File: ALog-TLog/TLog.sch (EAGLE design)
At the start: 107 parts, among them IC1 ATMEGA644M, J6 5.5x2.1mm Barrel, Q11 MOSFET-NCH-BSS138, Q12 MOSFET_PCH-IRLML2244, Q5 MOSFET_PCH-IRLML2244, Q6 MOSFET_PCH-IRLML2244, Q7 MOSFET_PCH-IRLML2244, Q8 MOSFET-NCH-BSS138, Q9 MOSFET-NCH-BSS138, U2 FT231X-Q, U3 915MHz, U4 SX1509, X2 87832-14

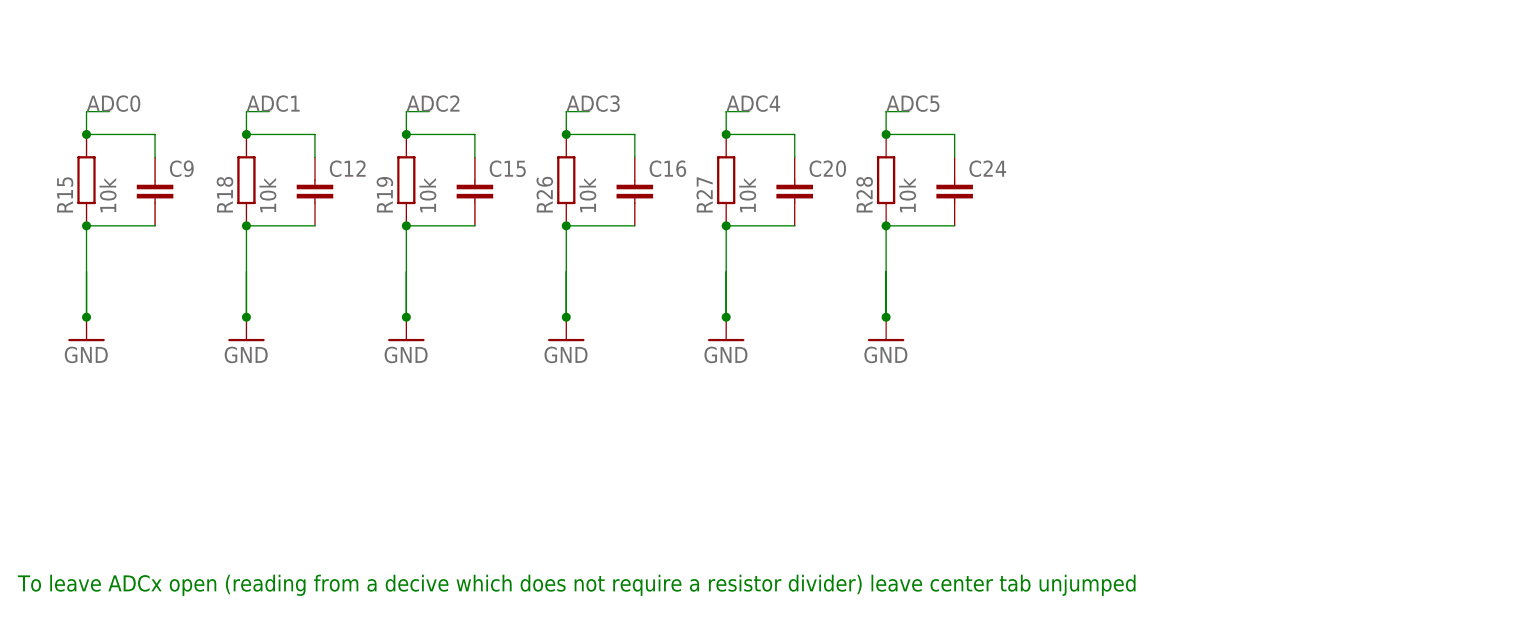
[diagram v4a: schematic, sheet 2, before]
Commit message: Issue Fix Complete
Fixed issues: #9, #12, #8

Ready for review
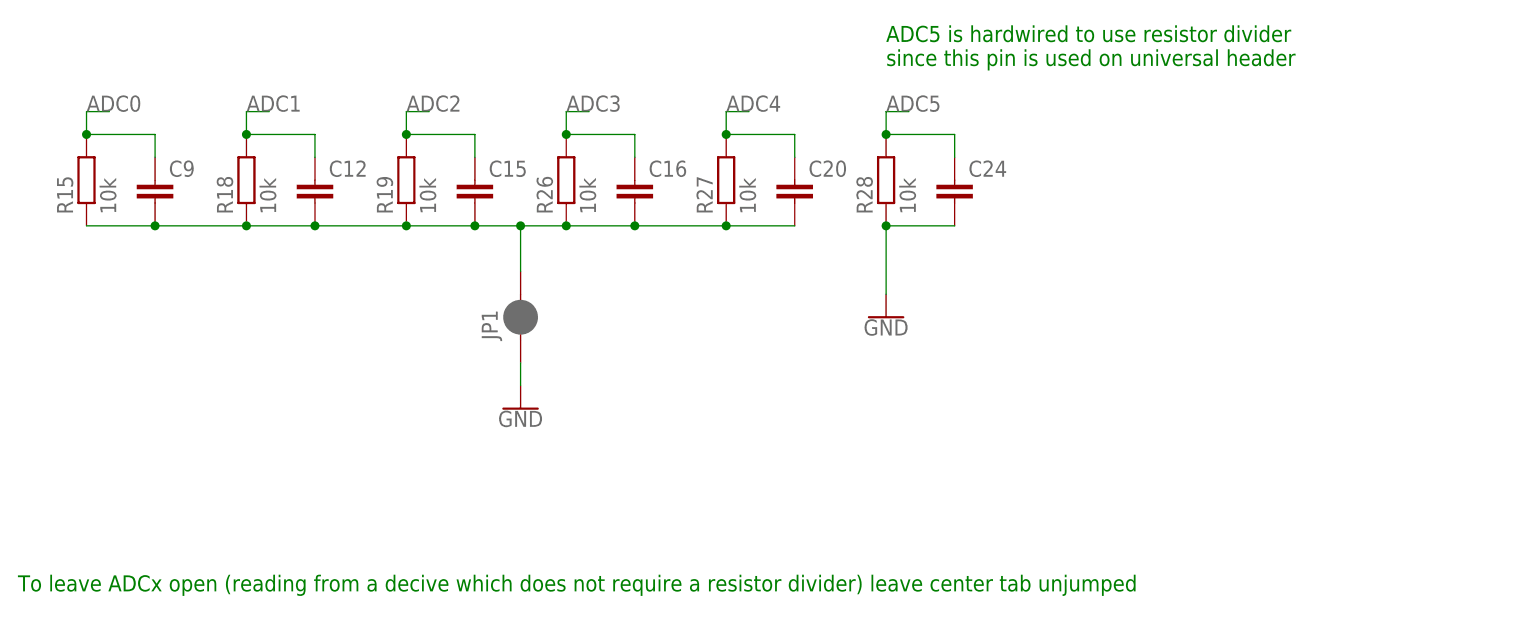
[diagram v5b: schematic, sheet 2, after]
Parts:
- added JP1: JUMPER-SMT_2_NC_PASTE_SILK, SparkFun-Jumpers:JUMPER-SMT_2_NC_PASTE_SILK
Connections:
- removed net 5V_EXT: R25.2
- new net THERM_GND: C12.2, C15.2, C16.2, C20.2, C9.2, JP1.2, R15.1, R18.1, R19.1, R26.1, R27.1
- net 5V: no longer U2.VCC
- net EXT_5V: now also R25.2
- net GND: now also JP1.1; no longer C12.2, C15.2, C16.2, C20.2, C9.2, R15.1, R18.1, R19.1, R26.1, R27.1
- net VUSB: now also U2.VCC
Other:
- note added: "ADC5 is hardwired to use resistor divider since this pin is used on universal header"
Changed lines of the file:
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@@
 <part name="GND24" library="supply1" library_urn="urn:adsk.eagle:library:371" deviceset="GND" device=""/>
 <part name="GND25" library="supply1" library_urn="urn:adsk.eagle:library:371" deviceset="GND" device=""/>
-<part name="GND26" library="supply1" library_urn="urn:adsk.eagle:library:371" deviceset="GND" device=""/>
-<part name="GND27" library="supply1" library_urn="urn:adsk.eagle:library:371" deviceset="GND" device=""/>
-<part name="GND28" library="supply1" library_urn="urn:adsk.eagle:library:371" deviceset="GND" device=""/>
-<part name="GND29" library="supply1" library_urn="urn:adsk.eagle:library:371" deviceset="GND" device=""/>
-<part name="GND30" library="supply1" library_urn="urn:adsk.eagle:library:371" deviceset="GND" device=""/>
-<part name="GND31" library="supply1" library_urn="urn:adsk.eagle:library:371" deviceset="GND" device=""/>
 <part name="J8" library="bschulz" deviceset="CONN_10" device="3.5MM">
 <attribute name="DIGIKEY" value="ED2735-ND"/>
@@
 <part name="C20" library="bschulz_passives" deviceset="C-EU" device="C0603"/>
 <part name="C24" library="bschulz_passives" deviceset="C-EU" device="C0603"/>
+<part name="GND14" library="SparkFun-PowerSymbols" library_urn="urn:adsk.eagle:library:530" deviceset="GND" device=""/>
+<part name="JP1" library="SparkFun-Jumpers" library_urn="urn:adsk.eagle:library:528" deviceset="JUMPER-SMT_2_NC_PASTE" device="_SILK" package3d_urn="urn:adsk.eagle:package:39282/1"/>
+<part name="GND17" library="SparkFun-PowerSymbols" library_urn="urn:adsk.eagle:library:530" deviceset="GND" device=""/>
 </parts>
 <sheets>
@@
 <net name="5V" class="0">
 <segment>
-<pinref part="U2" gate="G$1" pin="VCC"/>
-<pinref part="U$14" gate="G$1" pin="VUSB"/>
-<wire x1="279.4" y1="109.22" x2="279.4" y2="106.68" width="0.1524" layer="91"/>
-</segment>
-<segment>
 <wire x1="311.912" y1="38.1" x2="297.18" y2="38.1" width="0.1524" layer="91"/>
 <wire x1="297.18" y1="38.1" x2="297.18" y2="40.64" width="0.1524" layer="91"/>
@@
 <junction x="223.52" y="109.22"/>
 </segment>
+<segment>
+<pinref part="U2" gate="G$1" pin="VCC"/>
+<pinref part="U$14" gate="G$1" pin="VUSB"/>
+<wire x1="279.4" y1="109.22" x2="279.4" y2="106.68" width="0.1524" layer="91"/>
+</segment>
 </net>
 <net name="N$34" class="0">
@@
 <plain>
 <text x="22.86" y="35.56" size="1.778" layer="91">To leave ADCx open (reading from a decive which does not require a resistor divider) leave center tab unjumped</text>
+<text x="119.38" y="93.98" size="1.778" layer="91">ADC5 is hardwired to use resistor divider
+since this pin is used on universal header</text>
 </plain>
 <instances>
-<instance part="GND26" gate="1" x="30.48" y="63.5"/>
-<instance part="GND27" gate="1" x="48.26" y="63.5"/>
-<instance part="GND28" gate="1" x="66.04" y="63.5"/>
-<instance part="GND29" gate="1" x="83.82" y="63.5"/>
-<instance part="GND30" gate="1" x="101.6" y="63.5"/>
-<instance part="GND31" gate="1" x="119.38" y="63.5"/>
 <instance part="R15" gate="G$1" x="30.48" y="81.28" rot="R90"/>
 <instance part="R18" gate="G$1" x="48.26" y="81.28" rot="R90"/>
@@
 <instance part="C20" gate="G$1" x="109.22" y="81.28"/>
 <instance part="C24" gate="G$1" x="127" y="81.28"/>
+<instance part="GND14" gate="1" x="78.74" y="55.88"/>
+<instance part="JP1" gate="G$1" x="78.74" y="66.04" smashed="yes" rot="R90">
+<attribute name="NAME" x="76.2" y="63.5" size="1.778" layer="95" font="vector" rot="R90"/>
+</instance>
+<instance part="GND17" gate="1" x="119.38" y="66.04"/>
 </instances>
 <busses>
@@
 </segment>
 </net>
-<net name="GND" class="0">
-<segment>
-<pinref part="GND26" gate="1" pin="GND"/>
-<wire x1="30.48" y1="71.12" x2="30.48" y2="66.04" width="0.1524" layer="91"/>
+<net name="THERM_GND" class="0">
+<segment>
 <pinref part="R15" gate="G$1" pin="1"/>
 <pinref part="C9" gate="G$1" pin="2"/>
 <wire x1="38.1" y1="76.2" x2="30.48" y2="76.2" width="0.1524" layer="91"/>
-<wire x1="30.48" y1="76.2" x2="30.48" y2="66.04" width="0.1524" layer="91"/>
-<junction x="30.48" y="76.2"/>
-<junction x="30.48" y="66.04"/>
-</segment>
-<segment>
-<pinref part="GND27" gate="1" pin="GND"/>
-<wire x1="48.26" y1="71.12" x2="48.26" y2="66.04" width="0.1524" layer="91"/>
 <pinref part="R18" gate="G$1" pin="1"/>
 <pinref part="C12" gate="G$1" pin="2"/>
 <wire x1="55.88" y1="76.2" x2="48.26" y2="76.2" width="0.1524" layer="91"/>
-<wire x1="48.26" y1="76.2" x2="48.26" y2="66.04" width="0.1524" layer="91"/>
-<junction x="48.26" y="76.2"/>
-<junction x="48.26" y="66.04"/>
-</segment>
-<segment>
-<pinref part="GND28" gate="1" pin="GND"/>
-<wire x1="66.04" y1="71.12" x2="66.04" y2="66.04" width="0.1524" layer="91"/>
 <pinref part="R19" gate="G$1" pin="1"/>
 <pinref part="C15" gate="G$1" pin="2"/>
 <wire x1="73.66" y1="76.2" x2="66.04" y2="76.2" width="0.1524" layer="91"/>
-<wire x1="66.04" y1="76.2" x2="66.04" y2="66.04" width="0.1524" layer="91"/>
-<junction x="66.04" y="76.2"/>
-<junction x="66.04" y="66.04"/>
-</segment>
-<segment>
-<pinref part="GND29" gate="1" pin="GND"/>
-<wire x1="83.82" y1="71.12" x2="83.82" y2="66.04" width="0.1524" layer="91"/>
 <pinref part="R26" gate="G$1" pin="1"/>
 <pinref part="C16" gate="G$1" pin="2"/>
 <wire x1="91.44" y1="76.2" x2="83.82" y2="76.2" width="0.1524" layer="91"/>
-<wire x1="83.82" y1="76.2" x2="83.82" y2="66.04" width="0.1524" layer="91"/>
+<pinref part="JP1" gate="G$1" pin="2"/>
+<wire x1="78.74" y1="71.12" x2="78.74" y2="76.2" width="0.1524" layer="91"/>
+<wire x1="78.74" y1="76.2" x2="83.82" y2="76.2" width="0.1524" layer="91"/>
 <junction x="83.82" y="76.2"/>
-<junction x="83.82" y="66.04"/>
-</segment>
-<segment>
-<pinref part="GND30" gate="1" pin="GND"/>
-<wire x1="101.6" y1="71.12" x2="101.6" y2="66.04" width="0.1524" layer="91"/>
+<wire x1="73.66" y1="76.2" x2="78.74" y2="76.2" width="0.1524" layer="91"/>
+<junction x="73.66" y="76.2"/>
+<junction x="78.74" y="76.2"/>
 <pinref part="R27" gate="G$1" pin="1"/>
 <pinref part="C20" gate="G$1" pin="2"/>
 <wire x1="109.22" y1="76.2" x2="101.6" y2="76.2" width="0.1524" layer="91"/>
-<wire x1="101.6" y1="76.2" x2="101.6" y2="66.04" width="0.1524" layer="91"/>
+<wire x1="91.44" y1="76.2" x2="101.6" y2="76.2" width="0.1524" layer="91"/>
+<junction x="91.44" y="76.2"/>
 <junction x="101.6" y="76.2"/>
-<junction x="101.6" y="66.04"/>
-</segment>
-<segment>
-<pinref part="GND31" gate="1" pin="GND"/>
-<wire x1="119.38" y1="71.12" x2="119.38" y2="66.04" width="0.1524" layer="91"/>
+<wire x1="55.88" y1="76.2" x2="66.04" y2="76.2" width="0.1524" layer="91"/>
+<junction x="55.88" y="76.2"/>
+<junction x="66.04" y="76.2"/>
+<wire x1="38.1" y1="76.2" x2="48.26" y2="76.2" width="0.1524" layer="91"/>
+<junction x="38.1" y="76.2"/>
+<junction x="48.26" y="76.2"/>
+</segment>
+</net>
+<net name="GND" class="0">
+<segment>
+<pinref part="GND14" gate="1" pin="GND"/>
+<pinref part="JP1" gate="G$1" pin="1"/>
+<wire x1="78.74" y1="58.42" x2="78.74" y2="60.96" width="0.1524" layer="91"/>
+</segment>
+<segment>
 <pinref part="R28" gate="G$1" pin="1"/>
 <pinref part="C24" gate="G$1" pin="2"/>
 <wire x1="127" y1="76.2" x2="119.38" y2="76.2" width="0.1524" layer="91"/>
-<wire x1="119.38" y1="76.2" x2="119.38" y2="66.04" width="0.1524" layer="91"/>
+<pinref part="GND17" gate="1" pin="GND"/>
+<wire x1="119.38" y1="68.58" x2="119.38" y2="76.2" width="0.1524" layer="91"/>
 <junction x="119.38" y="76.2"/>
-<junction x="119.38" y="66.04"/>
 </segment>
 </net>
@@
 </segment>
 </net>
-<net name="5V_EXT" class="0">
+<net name="EXT_5V" class="0">
 <segment>
 <pinref part="R25" gate="G$1" pin="2"/>

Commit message: Presumptive Mrk 1.2
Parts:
- C12, C15, C16, C20, C24, C9: value (none) -> 0.1uF; device bschulz_passives:C-EUC0603 -> bschulz_passives:C-EU0.1UFC0603
- C8: value (none) -> 0.1uF
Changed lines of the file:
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@@
 <grid distance="0.1" unitdist="inch" unit="inch" style="lines" multiple="1" display="no" altdistance="0.01" altunitdist="inch" altunit="inch"/>
 <layers>
-<layer number="1" name="Top" color="4" fill="1" visible="no" active="no"/>
-<layer number="2" name="Route2" color="1" fill="3" visible="no" active="no"/>
-<layer number="3" name="Route3" color="4" fill="3" visible="no" active="no"/>
-<layer number="4" name="Route4" color="1" fill="4" visible="no" active="no"/>
-<layer number="5" name="Route5" color="4" fill="4" visible="no" active="no"/>
-<layer number="6" name="Route6" color="1" fill="8" visible="no" active="no"/>
-<layer number="7" name="Route7" color="4" fill="8" visible="no" active="no"/>
-<layer number="8" name="Route8" color="1" fill="2" visible="no" active="no"/>
-<layer number="9" name="Route9" color="4" fill="2" visible="no" active="no"/>
-<layer number="10" name="Route10" color="1" fill="7" visible="no" active="no"/>
-<layer number="11" name="Route11" color="4" fill="7" visible="no" active="no"/>
-<layer number="12" name="Route12" color="1" fill="5" visible="no" active="no"/>
-<layer number="13" name="Route13" color="4" fill="5" visible="no" active="no"/>
-<layer number="14" name="Route14" color="1" fill="6" visible="no" active="no"/>
-<layer number="15" name="Route15" color="4" fill="6" visible="no" active="no"/>
-<layer number="16" name="Bottom" color="1" fill="1" visible="no" active="no"/>
-<layer number="17" name="Pads" color="2" fill="1" visible="no" active="no"/>
-<layer number="18" name="Vias" color="2" fill="1" visible="no" active="no"/>
-<layer number="19" name="Unrouted" color="6" fill="1" visible="no" active="no"/>
-<layer number="20" name="Dimension" color="15" fill="1" visible="no" active="no"/>
-<layer number="21" name="tPlace" color="7" fill="1" visible="no" active="no"/>
-<layer number="22" name="bPlace" color="7" fill="1" visible="no" active="no"/>
-<layer number="23" name="tOrigins" color="15" fill="1" visible="no" active="no"/>
-<layer number="24" name="bOrigins" color="15" fill="1" visible="no" active="no"/>
-<layer number="25" name="tNames" color="7" fill="1" visible="no" active="no"/>
-<layer number="26" name="bNames" color="7" fill="1" visible="no" active="no"/>
-<layer number="27" name="tValues" color="7" fill="1" visible="no" active="no"/>
-<layer number="28" name="bValues" color="7" fill="1" visible="no" active="no"/>
+<layer number="1" name="Top" color="4" fill="1" visible="yes" active="no"/>
+<layer number="2" name="Route2" color="1" fill="3" visible="yes" active="no"/>
+<layer number="3" name="Route3" color="4" fill="3" visible="yes" active="no"/>
+<layer number="4" name="Route4" color="1" fill="4" visible="yes" active="no"/>
+<layer number="5" name="Route5" color="4" fill="4" visible="yes" active="no"/>
+<layer number="6" name="Route6" color="1" fill="8" visible="yes" active="no"/>
+<layer number="7" name="Route7" color="4" fill="8" visible="yes" active="no"/>
+<layer number="8" name="Route8" color="1" fill="2" visible="yes" active="no"/>
+<layer number="9" name="Route9" color="4" fill="2" visible="yes" active="no"/>
+<layer number="10" name="Route10" color="1" fill="7" visible="yes" active="no"/>
+<layer number="11" name="Route11" color="4" fill="7" visible="yes" active="no"/>
+<layer number="12" name="Route12" color="1" fill="5" visible="yes" active="no"/>
+<layer number="13" name="Route13" color="4" fill="5" visible="yes" active="no"/>
+<layer number="14" name="Route14" color="1" fill="6" visible="yes" active="no"/>
+<layer number="15" name="Route15" color="4" fill="6" visible="yes" active="no"/>
+<layer number="16" name="Bottom" color="1" fill="1" visible="yes" active="no"/>
+<layer number="17" name="Pads" color="2" fill="1" visible="yes" active="no"/>
+<layer number="18" name="Vias" color="2" fill="1" visible="yes" active="no"/>
+<layer number="19" name="Unrouted" color="6" fill="1" visible="yes" active="no"/>
+<layer number="20" name="Dimension" color="15" fill="1" visible="yes" active="no"/>
+<layer number="21" name="tPlace" color="7" fill="1" visible="yes" active="no"/>
+<layer number="22" name="bPlace" color="7" fill="1" visible="yes" active="no"/>
+<layer number="23" name="tOrigins" color="15" fill="1" visible="yes" active="no"/>
+<layer number="24" name="bOrigins" color="15" fill="1" visible="yes" active="no"/>
+<layer number="25" name="tNames" color="7" fill="1" visible="yes" active="no"/>
+<layer number="26" name="bNames" color="7" fill="1" visible="yes" active="no"/>
+<layer number="27" name="tValues" color="7" fill="1" visible="yes" active="no"/>
+<layer number="28" name="bValues" color="7" fill="1" visible="yes" active="no"/>
 <layer number="29" name="tStop" color="7" fill="3" visible="no" active="no"/>
 <layer number="30" name="bStop" color="7" fill="6" visible="no" active="no"/>
@@
 <layer number="35" name="tGlue" color="7" fill="4" visible="no" active="no"/>
 <layer number="36" name="bGlue" color="7" fill="5" visible="no" active="no"/>
-<layer number="37" name="tTest" color="7" fill="1" visible="no" active="no"/>
-<layer number="38" name="bTest" color="7" fill="1" visible="no" active="no"/>
+<layer number="37" name="tTest" color="7" fill="1" visible="yes" active="no"/>
+<layer number="38" name="bTest" color="7" fill="1" visible="yes" active="no"/>
 <layer number="39" name="tKeepout" color="4" fill="11" visible="no" active="no"/>
 <layer number="40" name="bKeepout" color="1" fill="11" visible="no" active="no"/>
@@
 <layer number="44" name="Drills" color="7" fill="1" visible="no" active="no"/>
 <layer number="45" name="Holes" color="7" fill="1" visible="no" active="no"/>
-<layer number="46" name="Milling" color="3" fill="1" visible="no" active="no"/>
-<layer number="47" name="Measures" color="7" fill="1" visible="no" active="no"/>
-<layer number="48" name="Document" color="7" fill="1" visible="no" active="no"/>
-<layer number="49" name="Reference" color="7" fill="1" visible="no" active="no"/>
-<layer number="50" name="dxf" color="7" fill="1" visible="no" active="no"/>
-<layer number="51" name="tDocu" color="7" fill="1" visible="no" active="no"/>
-<layer number="52" name="bDocu" color="7" fill="1" visible="no" active="no"/>
-<layer number="53" name="tGND_GNDA" color="7" fill="9" visible="no" active="no"/>
-<layer number="54" name="bGND_GNDA" color="1" fill="9" visible="no" active="no"/>
-<layer number="56" name="wert" color="7" fill="1" visible="no" active="no"/>
-<layer number="57" name="tCAD" color="7" fill="1" visible="no" active="no"/>
-<layer number="59" name="tCarbon" color="7" fill="1" visible="no" active="no"/>
-<layer number="60" name="bCarbon" color="7" fill="1" visible="no" active="no"/>
+<layer number="46" name="Milling" color="3" fill="1" visible="yes" active="no"/>
+<layer number="47" name="Measures" color="7" fill="1" visible="yes" active="no"/>
+<layer number="48" name="Document" color="7" fill="1" visible="yes" active="no"/>
+<layer number="49" name="Reference" color="7" fill="1" visible="yes" active="no"/>
+<layer number="50" name="dxf" color="7" fill="1" visible="yes" active="no"/>
+<layer number="51" name="tDocu" color="7" fill="1" visible="yes" active="no"/>
+<layer number="52" name="bDocu" color="7" fill="1" visible="yes" active="no"/>
+<layer number="53" name="tGND_GNDA" color="7" fill="9" visible="yes" active="no"/>
+<layer number="54" name="bGND_GNDA" color="1" fill="9" visible="yes" active="no"/>
+<layer number="56" name="wert" color="7" fill="1" visible="yes" active="no"/>
+<layer number="57" name="tCAD" color="7" fill="1" visible="yes" active="no"/>
+<layer number="59" name="tCarbon" color="7" fill="1" visible="yes" active="no"/>
+<layer number="60" name="bCarbon" color="7" fill="1" visible="yes" active="no"/>
 <layer number="90" name="Modules" color="5" fill="1" visible="yes" active="yes"/>
 <layer number="91" name="Nets" color="2" fill="1" visible="yes" active="yes"/>
@@
 <part name="GND7" library="SparkFun-PowerSymbols" library_urn="urn:adsk.eagle:library:530" deviceset="GND" device=""/>
 <part name="C7" library="bschulz" deviceset="C-EU" device="C0805" technology="10UF" value="10uF"/>
-<part name="C8" library="bschulz" deviceset="C-EU" device="C0603"/>
+<part name="C8" library="bschulz" deviceset="C-EU" device="C0603" value="0.1uF"/>
 <part name="J9" library="bschulz" deviceset="CONN_10" device="3.5MM">
 <attribute name="DIGIKEY" value="ED2735-ND"/>
@@
 <part name="GND21" library="supply1" deviceset="GND" device=""/>
 <part name="R22" library="rcl" deviceset="R-EU_" device="R0603" value="10k"/>
-<part name="C9" library="bschulz_passives" deviceset="C-EU" device="C0603"/>
-<part name="C12" library="bschulz_passives" deviceset="C-EU" device="C0603"/>
-<part name="C15" library="bschulz_passives" deviceset="C-EU" device="C0603"/>
-<part name="C16" library="bschulz_passives" deviceset="C-EU" device="C0603"/>
-<part name="C20" library="bschulz_passives" deviceset="C-EU" device="C0603"/>
-<part name="C24" library="bschulz_passives" deviceset="C-EU" device="C0603"/>
+<part name="C9" library="bschulz_passives" deviceset="C-EU" device="C0603" technology="0.1UF" value="0.1uF"/>
+<part name="C12" library="bschulz_passives" deviceset="C-EU" device="C0603" technology="0.1UF" value="0.1uF"/>
+<part name="C15" library="bschulz_passives" deviceset="C-EU" device="C0603" technology="0.1UF" value="0.1uF"/>
+<part name="C16" library="bschulz_passives" deviceset="C-EU" device="C0603" technology="0.1UF" value="0.1uF"/>
+<part name="C20" library="bschulz_passives" deviceset="C-EU" device="C0603" technology="0.1UF" value="0.1uF"/>
+<part name="C24" library="bschulz_passives" deviceset="C-EU" device="C0603" technology="0.1UF" value="0.1uF"/>
 <part name="GND14" library="SparkFun-PowerSymbols" library_urn="urn:adsk.eagle:library:530" deviceset="GND" device=""/>
 <part name="JP1" library="SparkFun-Jumpers" library_urn="urn:adsk.eagle:library:528" deviceset="JUMPER-SMT_2_NC_PASTE" device="_SILK" package3d_urn="urn:adsk.eagle:package:39282/1"/>
